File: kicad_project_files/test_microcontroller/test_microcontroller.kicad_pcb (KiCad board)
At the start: 2 copper layers, 53 x 80 mm, 41 parts, among them J1 USB_C_Receptacle_USB2.0, SW1 SW_Push, SW2 SW_Push, SW3 SW_Push, SW4 SW_Push, SW5 SW_Push, SW6 SW_Push, SW7 SW_Push, SW8 SW_Push, SW9 SW_Push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

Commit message: prof_pcb
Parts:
- removed REF** (x2): Jumper_THT, Liam_CustomFootprints:Jumper_THT
- added C4: 0.1uf, Capacitor_THT:C_Rect_L7.0mm_W2.0mm_P5.00mm, F.Cu at (162.4, 46.5)
- SW2, SW3, SW4, SW5, SW6, SW7, SW8, SW9, SW_CAPS1: footprint Button_Switch_THT:SW_PUSH_6mm -> Button - Alternate:SW_4-1437565-0
- moved R7 124.5 mm to (180.9, 35.0), turned to 0 degrees
- moved D_CAPS1 117.9 mm to (157.8, 65.7), turned to 0 degrees
- moved C7 114.1 mm to (158.3, 61.9)
- moved D6 111.9 mm to (146.5, 35.2), turned to 0 degrees
- moved C6 107.3 mm to (148.6, 68.9)
- moved R6 105.8 mm to (172.3, 43.1), turned to 0 degrees
- moved C3 104.1 mm to (164.1, 43.0), turned to 0 degrees
- moved R_CAPS1 100.9 mm to (150.2, 61.9), turned to 0 degrees
- moved R3 100.1 mm to (170.7, 46.4), turned to 0 degrees
- moved C1 98.6 mm to (155.5, 43.0), turned to 0 degrees
- moved R4 97.1 mm to (159.3, 54.1), turned to 0 degrees
- moved D3 93.6 mm to (120.2, 52.0), turned to 0 degrees
- moved R2 90.2 mm to (162.1, 49.9), turned to 0 degrees
- moved D2 87.6 mm to (120.2, 55.5), turned to 0 degrees
- moved R5 86.0 mm to (148.5, 65.8), turned to 0 degrees
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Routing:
- net ROW3: track 122.3 -> 0.00 mm
- net ROW2: track 105.3 -> 0.00 mm
- net ROW1: track 89.7 -> 0.00 mm
- net VCC: track 78.4 -> 0.00 mm
- net COL1: track 53.3 -> 0.00 mm
- net COL2: track 44.1 -> 0.00 mm
- net COL3: track 40.5 -> 0.00 mm
- net RESET: track 29.7 -> 0.00 mm
- net CAPS: track 18.4 -> 0.00 mm
- net Net-(C6-Pad2): track 13.1 -> 0.00 mm
- net D+: track 12.3 -> 0.00 mm
- net Net-(C7-Pad2): track 12.0 -> 0.00 mm
- net D-: track 11.3 -> 0.00 mm
- net Net-(J1-PadS1): track 11.3 -> 0.00 mm
- net MISO: track 10.3 -> 0.00 mm
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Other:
- board size 53 x 80 mm -> 60 x 100 mm

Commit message: pcb v1
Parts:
- moved R7 129.8 mm to (53.0, 57.2), turned to -90 degrees
- moved C7 121.4 mm to (37.5, 50.0)
- moved R1 119.2 mm to (42.2, 34.5)
- moved C6 114.4 mm to (37.5, 41.5)
- moved D6 110.3 mm to (61.0, 104.9), turned to -90 degrees
- moved D_CAPS1 103.5 mm to (54.2, 66.8), turned to 180 degrees
- moved R6 95.3 mm to (77.8, 31.2), turned to -90 degrees
- moved C4 95.2 mm to (67.2, 44.0), turned to -90 degrees
- moved R_CAPS1 94.8 mm to (55.5, 57.2), turned to -90 degrees
- moved D3 93.2 mm to (43.5, 104.9), turned to -90 degrees
- moved C3 92.4 mm to (71.7, 44.0), turned to -90 degrees
- moved R3 89.2 mm to (82.8, 31.2), turned to -90 degrees
- moved R4 87.1 mm to (75.2, 31.2), turned to -90 degrees
- moved D2 83.9 mm to (43.5, 89.7), turned to -90 degrees
- moved R2 79.2 mm to (86.5, 26.5)
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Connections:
- U1 pad 15: SCLK -> unconnected-(U1-Pad15)
- U1 pad 16: MOSI -> unconnected-(U1-Pad16)
- U1 pad 17: MISO -> unconnected-(U1-Pad17)
- U1 pad 6: unconnected-(U1-Pad6) -> MISO
- U1 pad 7: unconnected-(U1-Pad7) -> MOSI
- U1 pad 8: unconnected-(U1-Pad8) -> SCLK
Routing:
- net ROW3: track 0.00 -> 120.5 mm
- net ROW2: track 0.00 -> 103.6 mm
- net VCC: track 0.00 -> 92.0 mm, vias 0 -> 2
- net COL3: track 0.00 -> 79.1 mm, vias 0 -> 6
- net ROW1: track 0.00 -> 71.0 mm
- net COL2: track 0.00 -> 69.3 mm, vias 0 -> 6
- net COL1: track 0.00 -> 67.1 mm, vias 0 -> 6
- net SCLK: track 0.00 -> 49.5 mm, vias 0 -> 2
- net MOSI: track 0.00 -> 43.6 mm, vias 0 -> 2
- net RESET: track 0.00 -> 43.2 mm, vias 0 -> 2
- net MISO: track 0.00 -> 34.0 mm, vias 0 -> 2
- net D-: track 0.00 -> 33.9 mm, vias 0 -> 2
- net D+: track 0.00 -> 31.3 mm, vias 0 -> 2
- net Net-(J1-PadS1): track 0.00 -> 20.2 mm
- net Net-(C7-Pad2): track 0.00 -> 11.7 mm
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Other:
- board text added: "Keyboard Prototype v1 13/08/2022"

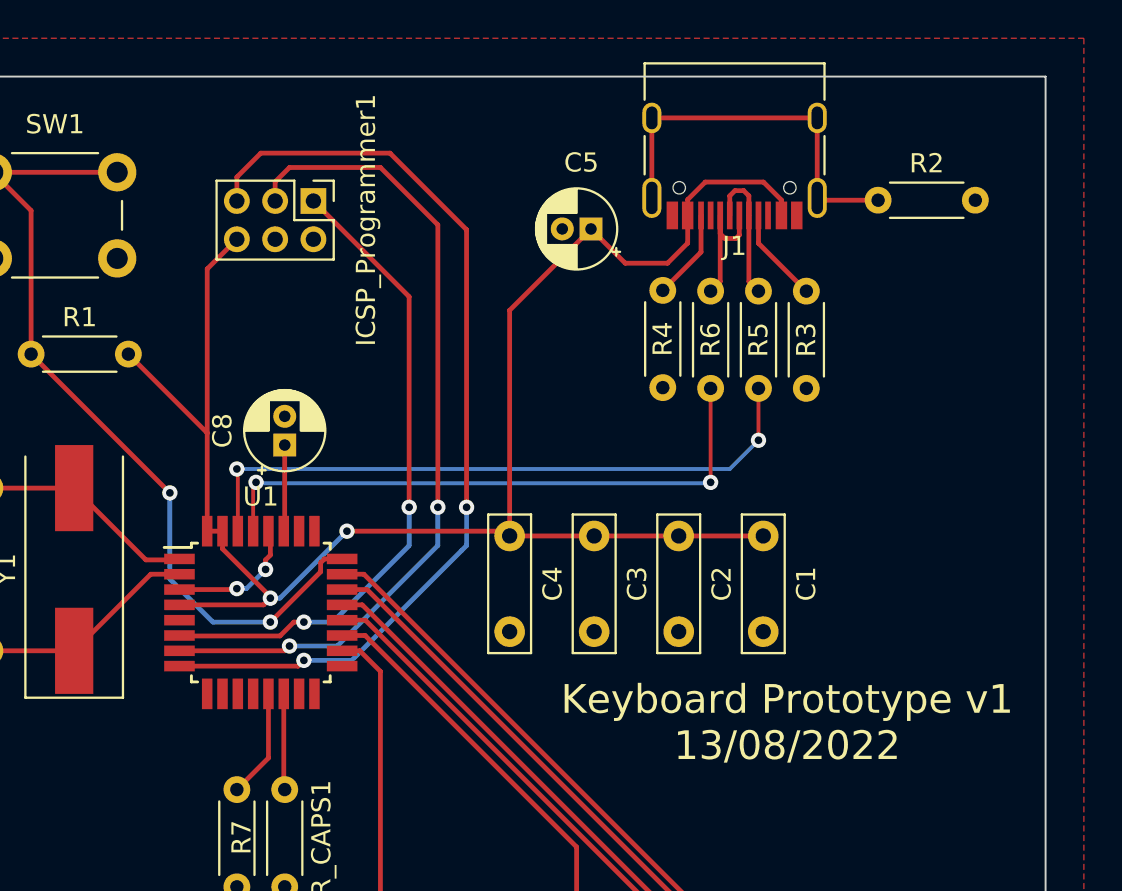
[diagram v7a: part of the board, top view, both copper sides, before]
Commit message: update Programming pin
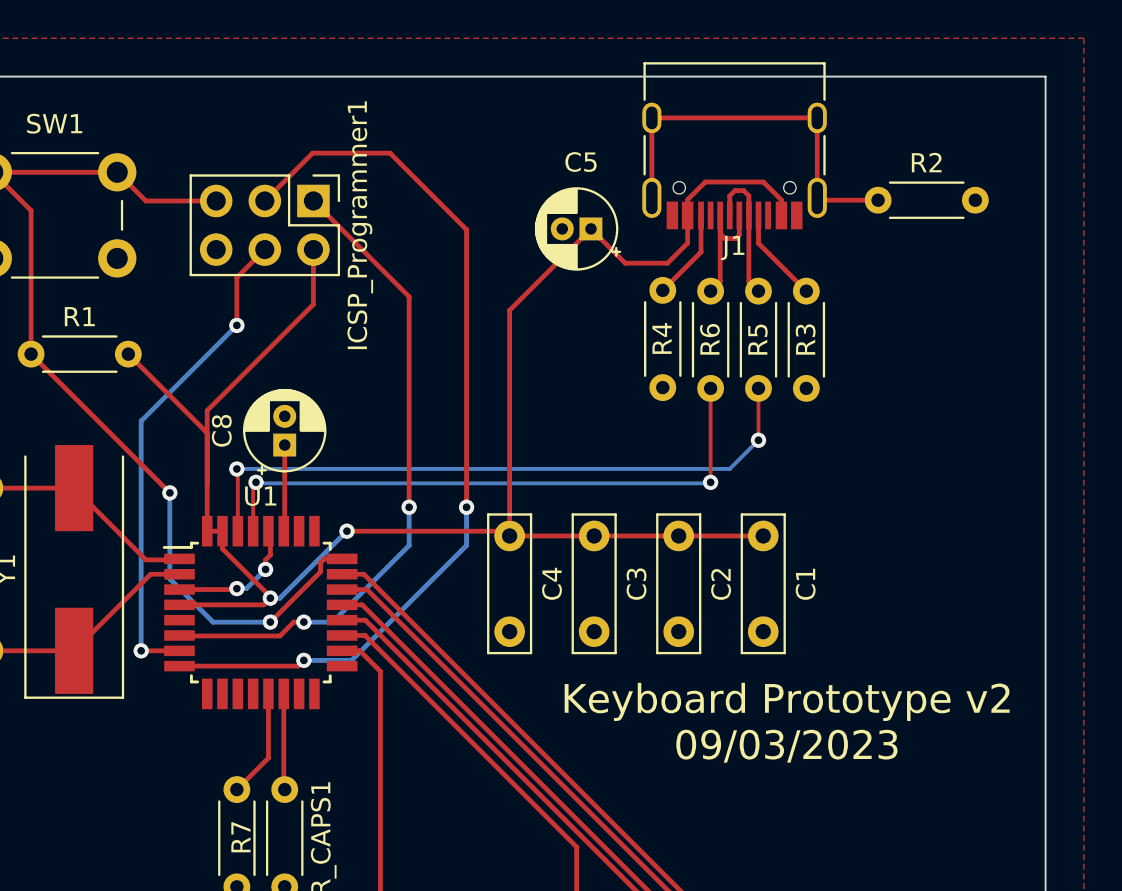
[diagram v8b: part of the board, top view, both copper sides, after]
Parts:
- ICSP_Programmer1: footprint Connector_PinHeader_2.00mm:PinHeader_2x03_P2.00mm_Vertical -> Connector_PinHeader_2.54mm:PinHeader_2x03_P2.54mm_Vertical
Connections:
- ICSP_Programmer1 pad 2: GND -> VCC
- ICSP_Programmer1 pad 3: MOSI -> SCLK
- ICSP_Programmer1 pad 4: unconnected-(ICSP_Programmer1-Pad4) -> MOSI
- ICSP_Programmer1 pad 5: SCLK -> RESET
- ICSP_Programmer1 pad 6: VCC -> GND
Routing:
- net MOSI: track 43.6 -> 25.6 mm
- net RESET: track 43.2 -> 48.9 mm
- net VCC: track 92.0 -> 95.8 mm
- net SCLK: track 49.5 -> 47.3 mm
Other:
- board text added: "Keyboard Prototype v2 09/03/2023"
- board text removed: "Keyboard Prototype v1 13/08/2022"
